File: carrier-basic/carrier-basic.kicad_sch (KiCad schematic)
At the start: 11 parts, among them J1 Conn_02x20_Counter_Clockwise, J2 Conn_02x20_Counter_Clockwise, J3 Conn_02x20_Counter_Clockwise, J4 Conn_02x20_Counter_Clockwise, J5 Conn_02x20_Counter_Clockwise, J6 Conn_02x20_Counter_Clockwise, J7 Conn_02x20_Counter_Clockwise

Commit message: Experiment with how I want to place some I/O on the basic carrier
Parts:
- added J10, J11, J12, J13, J8, J9: Conn_02x06_Odd_Even, Connector_PinSocket_2.54mm:PinSocket_2x06_P2.54mm_Horizontal, symbol Connector_Generic:Conn_02x06_Odd_Even
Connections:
- net +3V3: now also J10.1 (Pin_1), J10.2 (Pin_2), J11.1 (Pin_1), J11.2 (Pin_2), J12.1 (Pin_1), J12.2 (Pin_2), J13.1 (Pin_1), J13.2 (Pin_2), J8.1 (Pin_1), J8.2 (Pin_2), J9.1 (Pin_1), J9.2 (Pin_2)
- net GND: now also J10.3 (Pin_3), J10.4 (Pin_4), J11.3 (Pin_3), J11.4 (Pin_4), J12.3 (Pin_3), J12.4 (Pin_4), J13.3 (Pin_3), J13.4 (Pin_4), J8.3 (Pin_3), J8.4 (Pin_4), J9.3 (Pin_3), J9.4 (Pin_4)

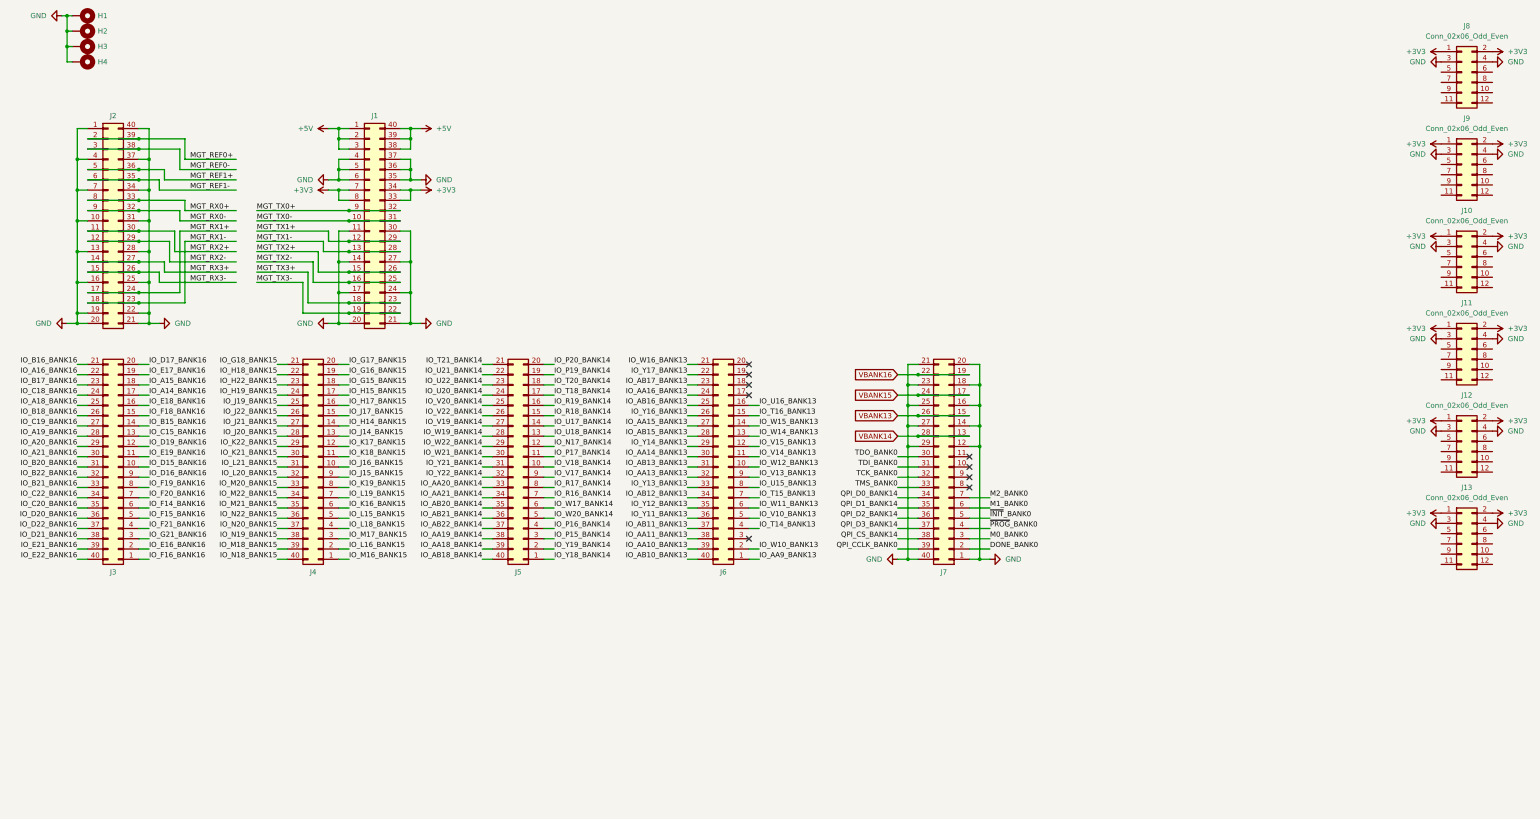
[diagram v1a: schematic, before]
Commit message: Make power traces on SOM thicker, more experimentallingification with carrier I/O layout
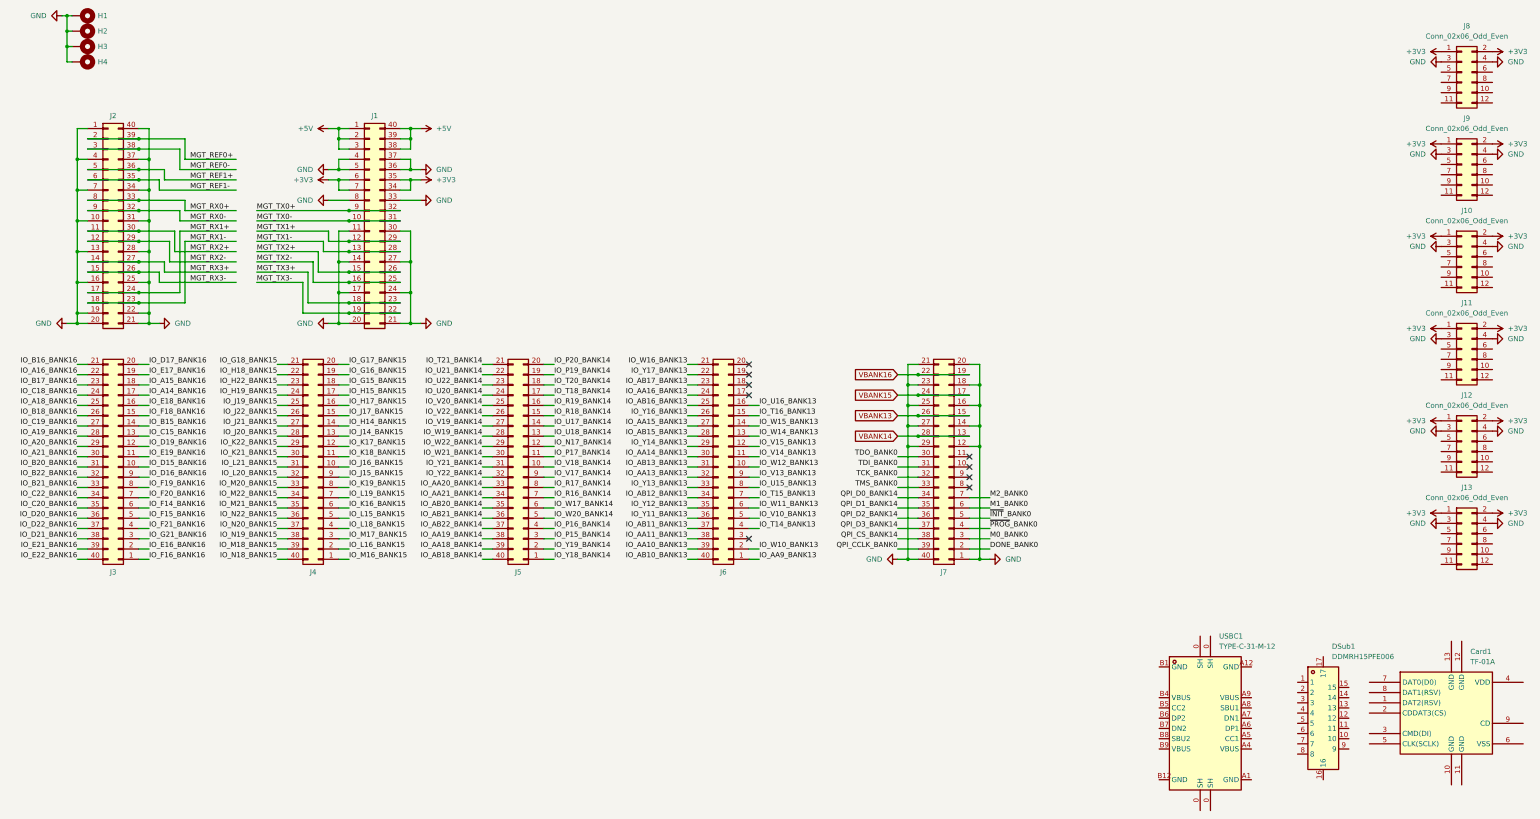
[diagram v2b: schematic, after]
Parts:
- added Card1: TF-01A, easyeda:TF-SMD_TF-01A, symbol easyeda:TF-01A
- added DSub1: DDMRH15PFE006, easyeda:DSUB-TH_15P-P2.29-H-F_DDMRH15PFE006, symbol easyeda:DDMRH15PFE006
- added USBC1: TYPE-C-31-M-12, easyeda:USB-C_SMD-TYPE-C-31-M-12, symbol easyeda:TYPE-C-31-M-12
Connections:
- net +3V3: now also J1.35 (Pin_35), J1.6 (Pin_6); no longer J1.33 (Pin_33), J1.8 (Pin_8)
- net GND: now also J1.33 (Pin_33), J1.8 (Pin_8); no longer J1.35 (Pin_35), J1.6 (Pin_6)

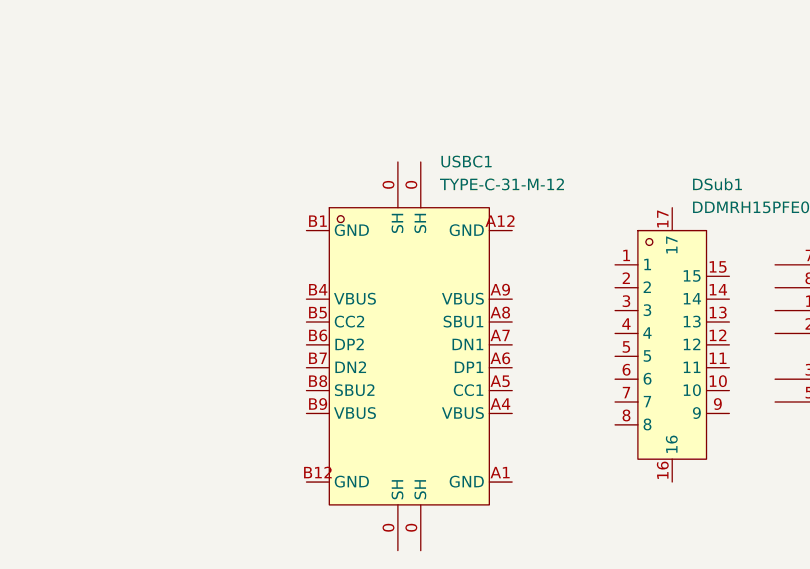
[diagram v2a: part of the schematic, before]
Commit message: Fix USB-C connector symbol and footprint
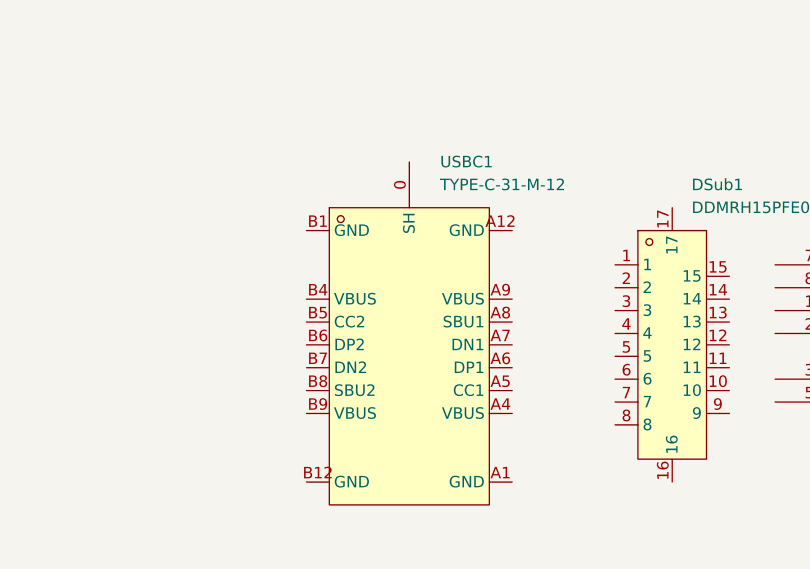
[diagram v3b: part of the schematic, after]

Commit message: Some more work on the carrier
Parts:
- added H5, H6, H7, H8: MountingHole_Pad, MountingHole:MountingHole_4mm_Pad, symbol Mechanical:MountingHole_Pad
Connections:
- net GND: now also H5.1, H6.1, H7.1, H8.1
